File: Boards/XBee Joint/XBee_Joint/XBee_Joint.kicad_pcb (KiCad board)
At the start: 4 copper layers, 25 x 48 mm, 40 parts, among them J1 SOICbite, J2 USB_C_Receptacle_USB2.0, U1 MCU_RaspberryPi_RP2040_RP2040, U2 AP2114H-3.3TRG1, U3 DRF1262TL, U4 W25Q128JVS, U5 USBLC6-2SC6, Y1 12MHz

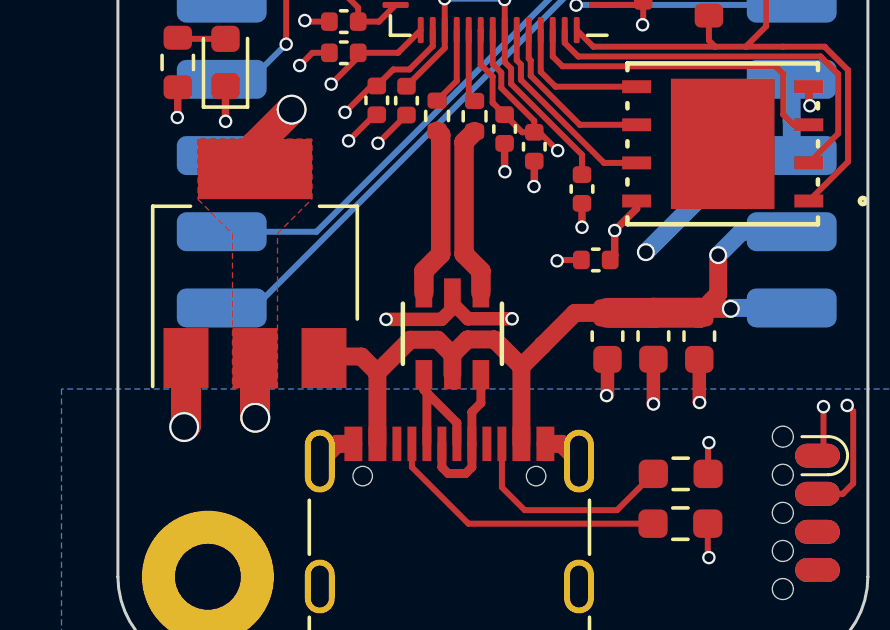
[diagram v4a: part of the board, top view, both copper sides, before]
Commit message: ordered new joint and bits
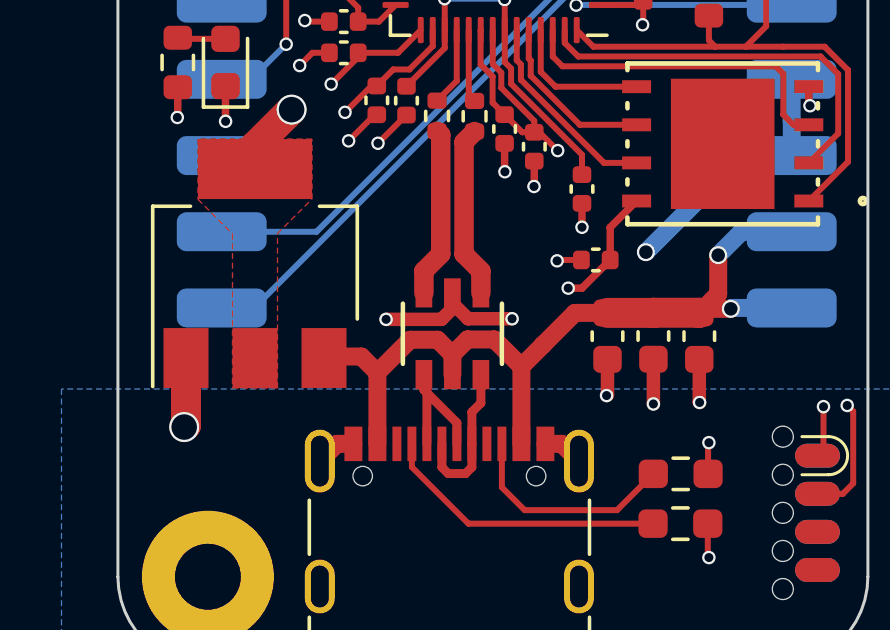
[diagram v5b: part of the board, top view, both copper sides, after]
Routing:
- net +3V3: track 43.7 -> 43.4 mm, vias 14 -> 13
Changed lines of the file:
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@@
   (segment (start 76.785 129.282552) (end 76.785 128.7475) (width 0.2) (layer "F.Cu") (net 3))
   (segment (start 68.28625 131.64375) (end 68.27 131.66) (width 0.25) (layer "F.Cu") (net 3))
-  (segment (start 82.85 135.43) (end 82.85 136.26) (width 0.25) (layer "F.Cu") (net 3))
   (segment (start 76.39 119.63) (end 75.45 118.69) (width 0.2) (layer "F.Cu") (net 3))
-  (segment (start 83.58 134.445) (end 83.58 134.7) (width 0.25) (layer "F.Cu") (net 3))
   (segment (start 78.785 129.88) (end 79.07 130.165) (width 0.2) (layer "F.Cu") (net 3))
   (segment (start 78.785 128.7475) (end 78.785 129.88) (width 0.2) (layer "F.Cu") (net 3))
+  (segment (start 82.7 136.41) (end 82.7 135.325) (width 0.25) (layer "F.Cu") (net 3))
   (segment (start 70.86 133.38) (end 70.86 132.62) (width 1) (layer "F.Cu") (net 3))
   (segment (start 74.3 128) (end 73.8 127.5) (width 0.2) (layer "F.Cu") (net 3))
@@
   (segment (start 74.3 125.128263) (end 75.118263 124.31) (width 0.2) (layer "F.Cu") (net 3))
   (segment (start 80.17 132.155) (end 80.34 132.155) (width 0.2) (layer "F.Cu") (net 3))
-  (segment (start 82.85 136.26) (end 82.7 136.41) (width 0.25) (layer "F.Cu") (net 3))
   (segment (start 74.3 128.465) (end 74.9925 128.465) (width 0.2) (layer "F.Cu") (net 3))
   (segment (start 74.08 125.39) (end 73.29 126.18) (width 0.2) (layer "F.Cu") (net 3))
@@
   (segment (start 80.17 132.155) (end 79.77 132.155) (width 0.2) (layer "F.Cu") (net 3))
   (segment (start 68.28625 130.6525) (end 68.28625 131.64375) (width 0.25) (layer "F.Cu") (net 3))
-  (segment (start 70.86 139.68) (end 70.86 141.66) (width 1) (layer "F.Cu") (net 3))
   (segment (start 78.385 128.7475) (end 78.38 128.7525) (width 0.2) (layer "F.Cu") (net 3))
   (segment (start 73.8 127.5) (end 73.34 127.5) (width 0.2) (layer "F.Cu") (net 3))
@@
   (segment (start 74.3 129.505) (end 75.6275 129.505) (width 0.2) (layer "F.Cu") (net 3))
   (segment (start 76.472 119.692) (end 77.694552 119.692) (width 0.2) (layer "F.Cu") (net 3))
+  (segment (start 81.76 137.35) (end 82.7 136.41) (width 0.25) (layer "F.Cu") (net 3))
   (segment (start 76.41 119.63) (end 76.39 119.63) (width 0.2) (layer "F.Cu") (net 3))
   (segment (start 74.3 129.505) (end 74.3 129.65) (width 0.2) (layer "F.Cu") (net 3))
@@
   (segment (start 83.8 127.79) (end 83.8 128.55) (width 0.2) (layer "F.Cu") (net 3))
   (segment (start 78.38 129.893055) (end 78.78 130.293055) (width 0.2) (layer "F.Cu") (net 3))
+  (segment (start 81.3 137.35) (end 81.76 137.35) (width 0.25) (layer "F.Cu") (net 3))
   (segment (start 79.07 130.675) (end 80.17 131.775) (width 0.2) (layer "F.Cu") (net 3))
   (segment (start 78.78 130.293055) (end 78.78 131.165) (width 0.2) (layer "F.Cu") (net 3))
@@
   (segment (start 74.92 130.61) (end 75.47 130.06) (width 0.2) (layer "F.Cu") (net 3))
   (segment (start 82.4225 124.31) (end 83.61 124.31) (width 0.2) (layer "F.Cu") (net 3))
+  (segment (start 82.7 135.325) (end 83.58 134.445) (width 0.25) (layer "F.Cu") (net 3))
   (segment (start 74.9925 128.465) (end 75.5475 127.91) (width 0.2) (layer "F.Cu") (net 3))
   (segment (start 78.785 120.782448) (end 78.785 121.8725) (width 0.2) (layer "F.Cu") (net 3))
-  (segment (start 70.86 141.66) (end 70.87 141.67) (width 1) (layer "F.Cu") (net 3))
-  (segment (start 83.58 134.7) (end 82.85 135.43) (width 0.25) (layer "F.Cu") (net 3))
   (segment (start 74.3 125.39) (end 74.3 125.128263) (width 0.2) (layer "F.Cu") (net 3))
   (segment (start 76.007552 130.06) (end 76.785 129.282552) (width 0.2) (layer "F.Cu") (net 3))
@@
   (via (at 73.4 130.55) (size 0.45) (drill 0.3) (layers "F.Cu" "B.Cu") (net 3))
   (via (at 83.78 128.57) (size 0.45) (drill 0.3) (layers "F.Cu" "B.Cu") (net 3))
-  (via (at 82.85 135.43) (size 0.45) (drill 0.3) (layers "F.Cu" "B.Cu") (net 3))
+  (via (at 81.3 137.35) (size 0.45) (drill 0.3) (layers "F.Cu" "B.Cu") (net 3))
   (via (at 73.29 126.18) (size 0.45) (drill 0.3) (layers "F.Cu" "B.Cu") (net 3))
   (via (at 68.27 131.66) (size 0.45) (drill 0.3) (layers "F.Cu" "B.Cu") (net 3))
@@
   (via (at 80.95 132.765) (size 0.45) (drill 0.3) (layers "F.Cu" "B.Cu") (net 3))
   (via (at 85.89 125.58) (size 0.45) (drill 0.3) (layers "F.Cu" "B.Cu") (net 3))
-  (via (at 70.87 141.67) (size 1) (drill 0.85) (layers "F.Cu" "B.Cu") (net 3))
   (via (at 73.86 131.49) (size 0.45) (drill 0.3) (layers "F.Cu" "B.Cu") (net 3))
   (via (at 72.08 131.4) (size 1) (drill 0.85) (layers "F.Cu" "B.Cu") (net 3))
@@
   )
   (zone (net 3) (net_name "+3V3") (layer "In1.Cu") (hatch edge 0.5)
-    (connect_pads yes (clearance 0.17))
+    (priority 3)
+    (connect_pads (clearance 0.17))
     (min_thickness 0.25) (filled_areas_thickness no)
     (fill yes (thermal_gap 0.5) (thermal_bridge_width 0.5))
     (polygon
       (pts
-        (xy 95.05 99.65)
-        (xy 64.17 99.65)
-        (xy 61.75 102.07)
-        (xy 61.75 148.77)
-        (xy 66.82 153.84)
-        (xy 95.05 153.84)
+        (xy 66.28 118)
+        (xy 80.82 118)
+        (xy 87.25 124.43)
+        (xy 87.25 129.5)
+        (xy 87.23 129.52)
+        (xy 81.82 129.52)
+        (xy 81.82 138.06)
+        (xy 81.8 138.08)
+        (xy 80.73 138.08)
+        (xy 78.76 136.11)
+        (xy 78.76 131.91)
+        (xy 77.71 130.86)
+        (xy 75.47 130.86)
+        (xy 73.19 133.14)
+        (xy 67.67 133.14)
+        (xy 65.14 130.61)
+        (xy 65.14 119.14)
       )
     )
+  )
+  (zone (net 1) (net_name "GND") (layer "In1.Cu") (hatch edge 0.5)
+    (connect_pads (clearance 0.17))
+    (min_thickness 0.25) (filled_areas_thickness no)
+    (fill yes (thermal_gap 0.5) (thermal_bridge_width 0.5))
+    (polygon
+      (pts
+        (xy 62.8 151.67)
+        (xy 98.02 151.67)
+        (xy 98.02 98.8)
+        (xy 96.31 97.09)
+        (xy 63.22 97.09)
+        (xy 61.51 98.8)
+        (xy 61.51 150.38)
+      )
+    )
